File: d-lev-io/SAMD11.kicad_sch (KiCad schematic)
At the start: 27 parts, among them J6 PROG_HDR, J7 TOUCH_HDR, SW1 SW_Push, SW2 SW_Push, SW3 SW_Push, U3 ATSAMD11D14A-M

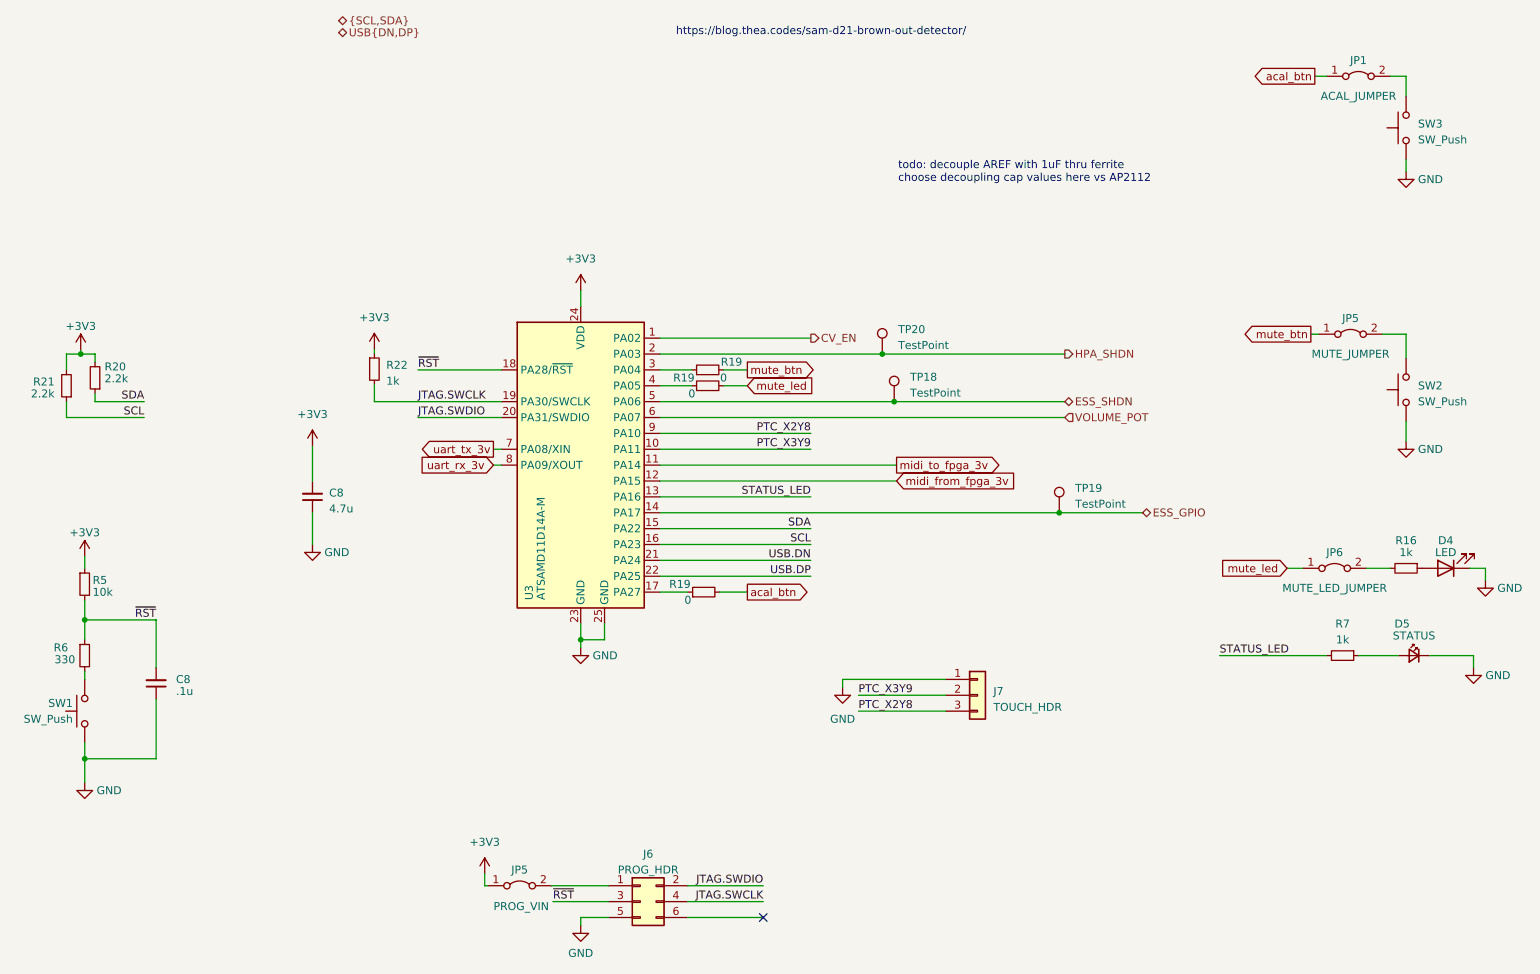
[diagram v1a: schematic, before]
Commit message: I/O board silk placement
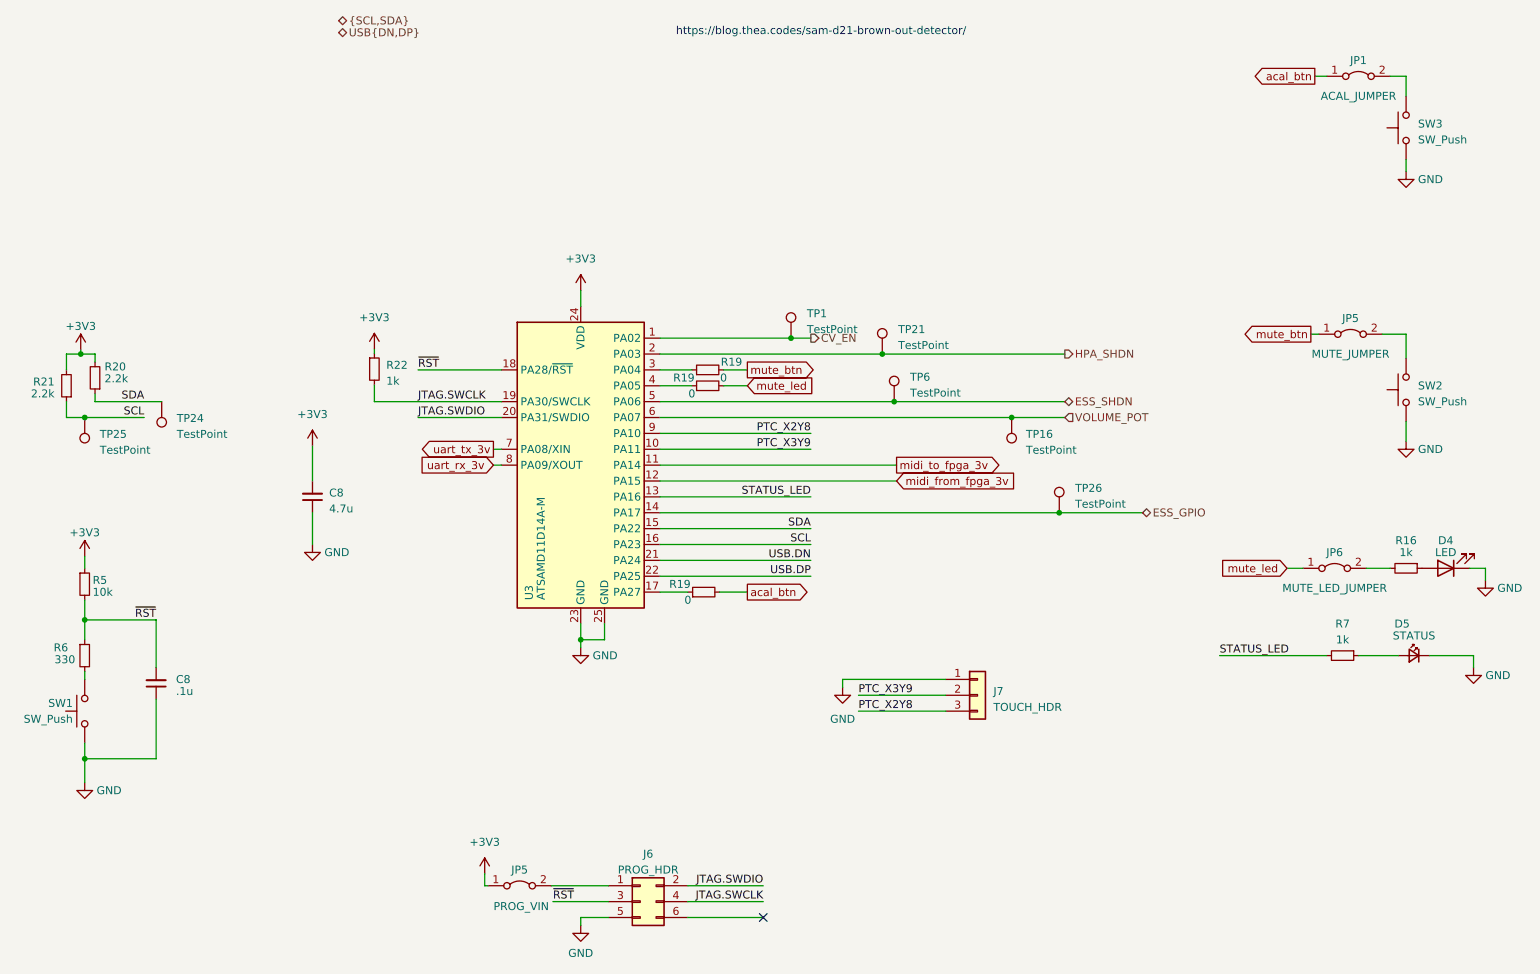
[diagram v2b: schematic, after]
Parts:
- added TP1, TP16, TP24, TP25: TestPoint, TestPoint:TestPoint_Pad_D1.5mm, symbol Connector:TestPoint
- renumbered TP20 to TP21, TP19 to TP26, TP18 to TP6
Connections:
- net CV_EN: now also TP1.1
- net SCL: now also TP25.1
- net SDA: now also TP24.1
- net VOLUME_POT: now also TP16.1
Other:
- note removed: "todo: decouple AREF with 1uF thru ferrite choose decoupling cap values here vs AP2112"

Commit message: Add iBOMs and additional part numbers
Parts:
- C8: MPN (none) -> CL10B475KQ8NQNC; Notes (none) -> Common; Supplier (none) -> Digi-Key; Supplier Alt (none) -> Mouser; Supplier Alt URL (none) -> https://www.mouser.com/ProductDetail/187-CL10B475KQ8NQNC; Supplier URL (none) -> https://www.digikey.com/en/products/detail/samsung-electro-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
- C8: value .1u -> 100n; MPN (none) -> GRM188R71E104KA01D; Notes (none) -> Common; Supplier (none) -> Digi-Key; Supplier URL (none) -> https://www.digikey.com/en/products/detail/murata-electroni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
- D4: MPN (none) -> 150060GS75000; Supplier (none) -> Mouser; Supplier URL (none) -> https://www.mouser.com/ProductDetail/710-150060GS75000
- D5: value STATUS -> LED; MPN (none) -> 150060GS75000; Supplier (none) -> Mouser; Supplier URL (none) -> https://www.mouser.com/ProductDetail/710-150060GS75000
- J6, J7, JP1, JP5, JP6, TP1, TP16, TP21, TP24, TP25, TP26, TP6: DNP (none) -> Y
- R19: MPN (none) -> RMCF0603ZT0R00; Supplier (none) -> Digi-Key; Supplier URL (none) -> https://www.digikey.com/en/products/detail/stackpole-electr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
- SW1, SW2, SW3: MPN (none) -> B3U-1000P; Supplier (none) -> Mouser; Supplier Alt (none) -> Amazon; Supplier Alt URL (none) -> https://www.amazon.com/Liyafy-Switch-3x4x2mm-Momentary-Tact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; Supplier URL (none) -> https://www.mouser.com/ProductDetail/653-B3U-1000P
- U3: MPN (none) -> ATSAMD11D14A-MUT; Supplier (none) -> Mouser; Supplier URL (none) -> https://www.mouser.com/ProductDetail/556-ATSAMD11D14A-MUT
